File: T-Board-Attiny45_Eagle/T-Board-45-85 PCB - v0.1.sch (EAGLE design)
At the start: 17 parts, among them IC1 LD117MIRROR, IC4 NCP1117MIRROR, J1 POWER_JACKPTH, J2 AVR_SPI_PRG_6PTH, U1 TINY45-20-DIP

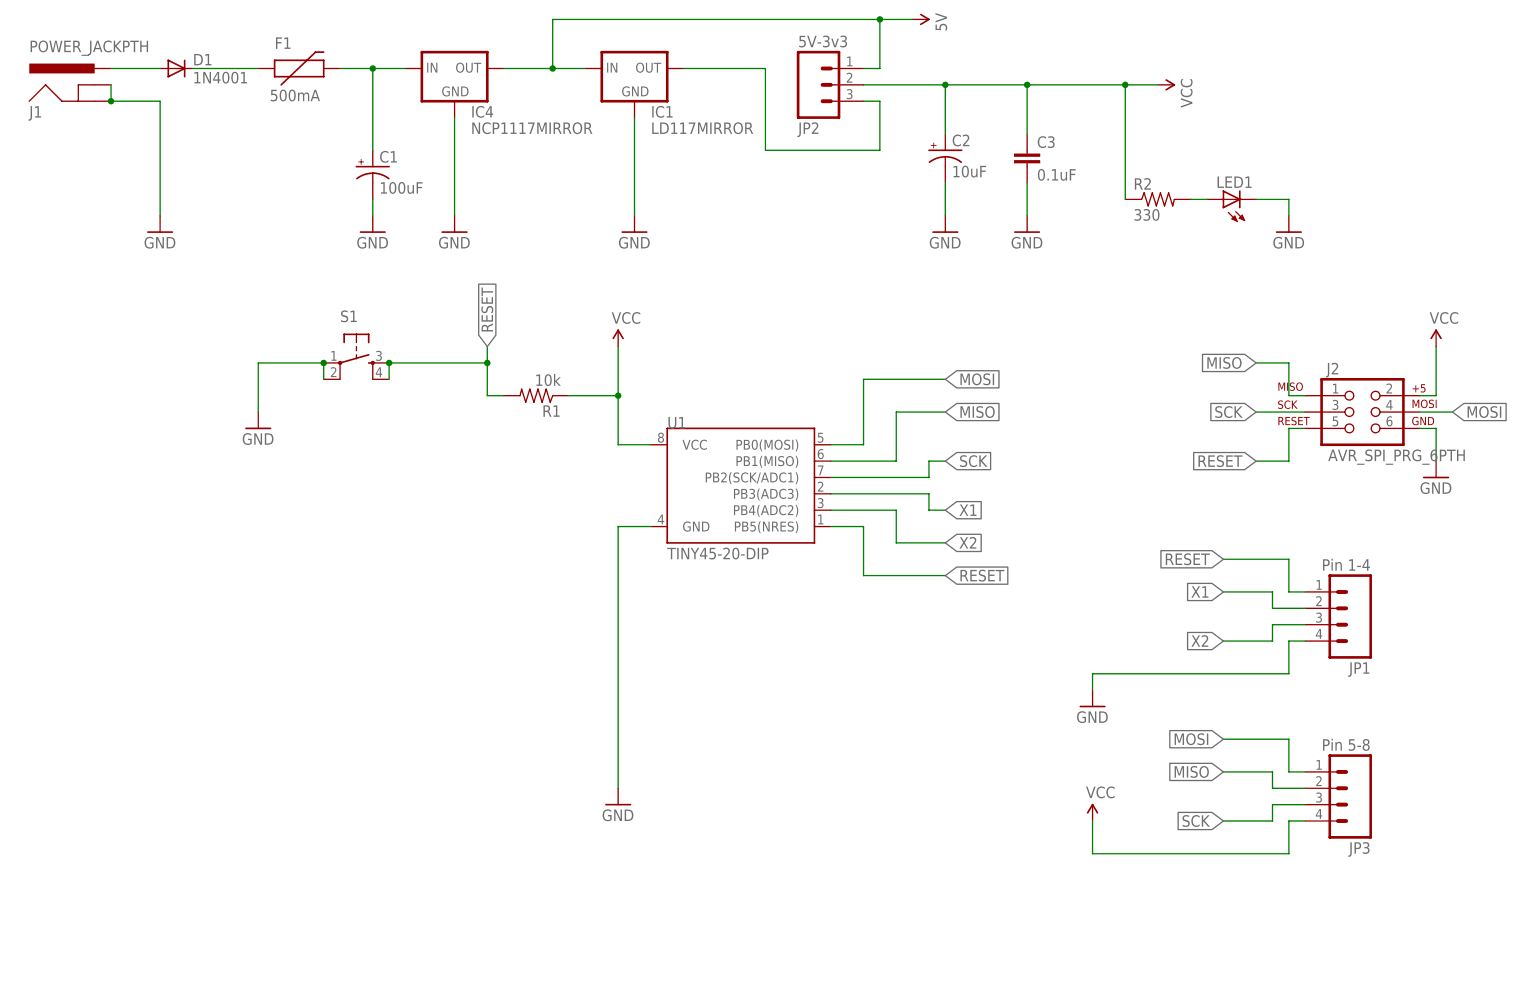
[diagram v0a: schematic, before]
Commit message: v0.2 - 2-sided prototype
2-sided prototype send to OSHPark to fab.  Includes:
- ICSP header
- Consistency in trace width
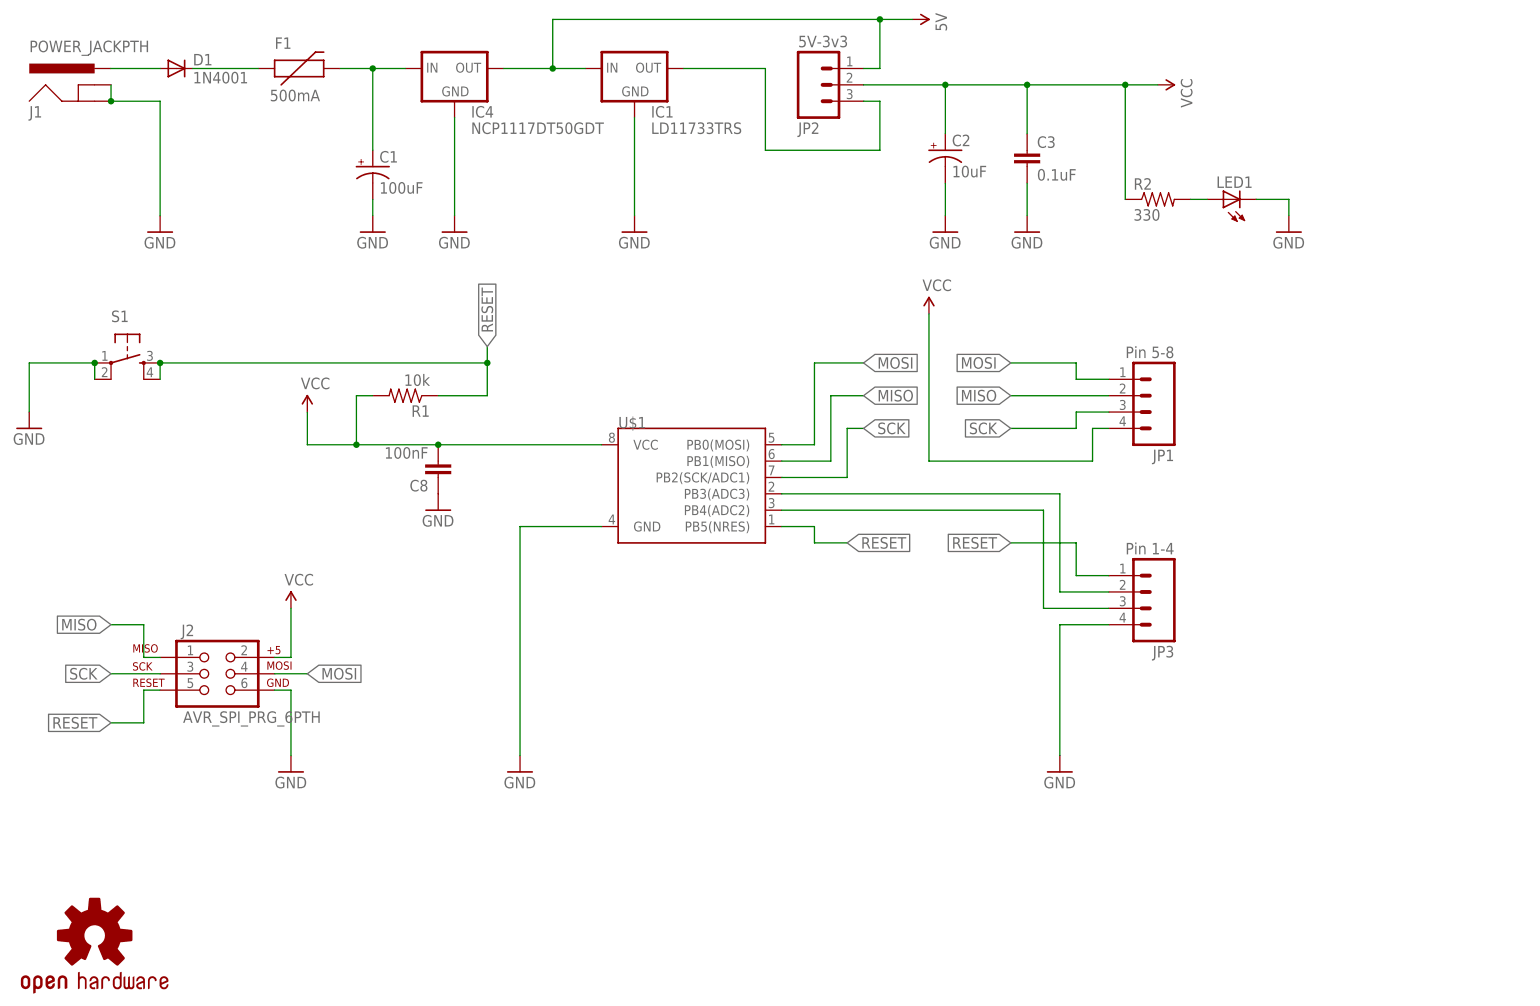
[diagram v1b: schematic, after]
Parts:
- removed U1: TINY45-20-DIP, SparkFun-DigitalIC:ATTINY45TINY45-20-DIP
- added C8: 100nF, SparkFun-Passives:CAP1206
- added LOGO1: OSHW-LOGOS, SparkFun-Aesthetics:OSHW-LOGOS
- added U$1: (no value), SparkFun-DigitalIC:ATTINY45TINY45-20-DIP
- IC1: value LD117MIRROR -> LD11733TRS; device AndyTallack:LD117MIRROR -> AndyTallack:LD11733TRS
- IC4: value NCP1117MIRROR -> NCP1117DT50GDT; device AndyTallack:NCP1117MIRROR -> AndyTallack:NCP1117DT50GDT
- JP1: value Pin 1-4 -> Pin 5-8
- JP3: value Pin 5-8 -> Pin 1-4
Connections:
- removed net X1: JP1.2, U1.PB3(ADC3)
- removed net X2: JP1.3, U1.PB4(ADC2)
- new net N$6: JP3.2, U$1.PB3(ADC3)
- new net N$7: JP3.3, U$1.PB4(ADC2)
- net GND: now also C8.1, JP3.4, U$1.GND; no longer JP1.4, U1.GND
- net MISO: now also JP1.2, U$1.PB1(MISO); no longer JP3.2, U1.PB1(MISO)
- net MOSI: now also JP1.1, U$1.PB0(MOSI); no longer JP3.1, U1.PB0(MOSI)
- net RESET: now also JP3.1, R1.1, U$1.PB5(NRES); no longer JP1.1, R1.2, U1.PB5(NRES)
- net SCK: now also JP1.3, U$1.PB2(SCK/ADC1); no longer JP3.3, U1.PB2(SCK/ADC1)
- net VCC: now also C8.2, JP1.4, R1.2, U$1.VCC; no longer JP3.4, R1.1, U1.VCC
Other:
- moved on the sheet: J2, JP1, JP3, R1, S1
